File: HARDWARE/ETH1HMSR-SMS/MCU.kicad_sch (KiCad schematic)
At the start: 27 parts, among them J401 20021111-00010T4LF, U401 STM32H743VITx, U402 24LC08B-E/MS, Y401 NX5032GA-16

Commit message: SW and HW development
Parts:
- added C415, C418: 1u, Capacitor_SMD:C_0603_1608Metric_Pad1.08x0.95mm_HandSolder, symbol Device:C
- added C416, C417: 0.1u, Capacitor_SMD:C_0603_1608Metric_Pad1.08x0.95mm_HandSolder, symbol Device:C
- added R407: 0, Resistor_SMD:R_0603_1608Metric_Pad0.98x0.95mm_HandSolder, symbol Device:R
- added U403: ADR4533, Package_SO:SOIC-8_3.9x4.9mm_P1.27mm, symbol Reference_Voltage:ADR4533
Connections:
- net GND: now also C415.2, C416.2, C417.2, C418.2, U403.4 (GND)
- net MCU_DEFAULT: now also U401.77 (PA15); no longer U401.22 (PA0)
- net VDDA: now also R407.2; no longer U401.20 (VREF+)
- net HMSR_VOUT: now reaches U401.18 (PC3_C)
- new net +3.3VADC: C417.1, C418.1, R407.1, U401.20 (VREF+), U403.6 (OUT)
- new net +5V: C415.1, C416.1, U403.2 (IN)
- no-connect marks 32 -> 30
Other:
- moved on the sheet: C406, C409, C410, C412, FB401, JP401, R401, R403

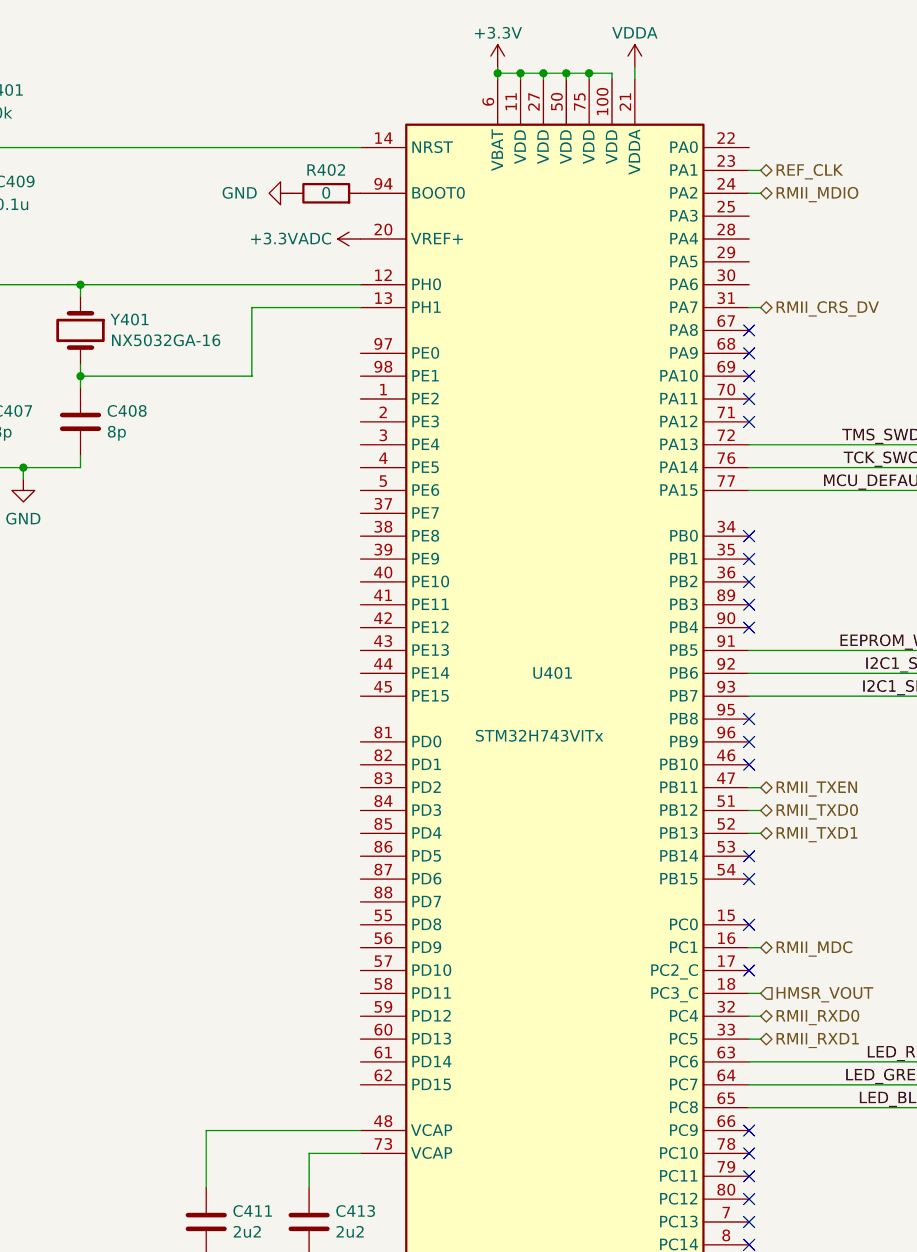
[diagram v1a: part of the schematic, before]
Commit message: Updated to Kicad 8
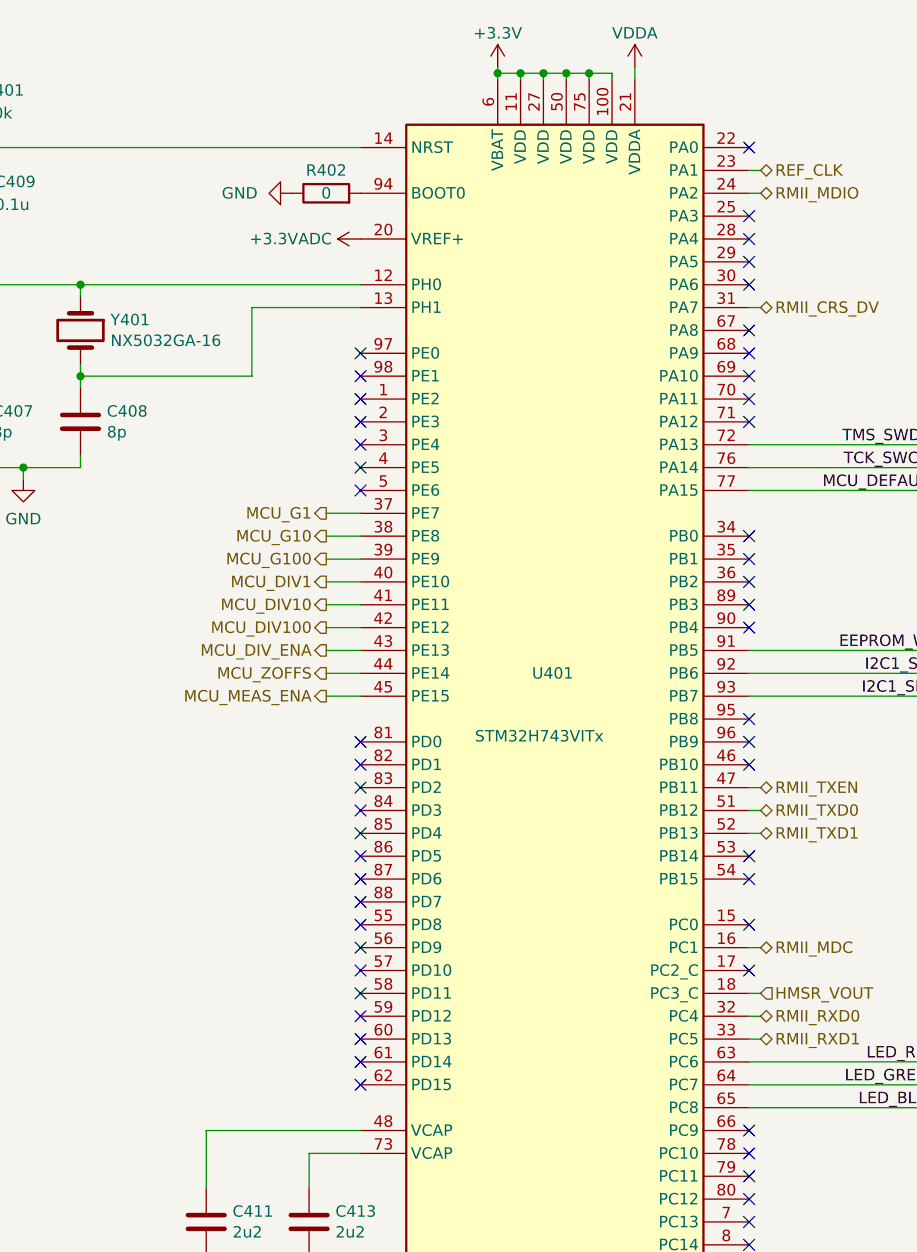
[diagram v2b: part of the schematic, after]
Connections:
- net MCU_G1: now reaches U401.37 (PE7)
- net MCU_G10: now reaches U401.38 (PE8)
- net MCU_G100: now reaches U401.39 (PE9)
- net MCU_DIV1: now reaches U401.40 (PE10)
- net MCU_DIV10: now reaches U401.41 (PE11)
- net MCU_DIV100: now reaches U401.42 (PE12)
- net MCU_DIV_ENA: now reaches U401.43 (PE13)
- net MCU_ZOFFS: now reaches U401.44 (PE14)
- net MCU_MEAS_ENA: now reaches U401.45 (PE15)
- no-connect marks 30 -> 58

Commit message: PCB design
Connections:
- net MCU_DEFAULT: no longer JP401.1 (A), R403.1, U401.77 (PA15)
- net MCU_DEF: now reaches U401.1 (PE2)
- net MCU_DEF: now also JP401.1 (A), R403.1
- no-connect marks 58 -> 57
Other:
- moved on the sheet: C401, C402, C403, C404, C405, C406, C407, C408, C409, C410, C411, C412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

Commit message: Development
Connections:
- net LED_BLUE: now also U401.63 (PC6); no longer U401.65 (PC8)
- net LED_GREEN: now also U401.65 (PC8); no longer U401.64 (PC7)
- net LED_RED: now also U401.64 (PC7); no longer U401.63 (PC6)
- net MCU_DIV1: now also U401.45 (PE15); no longer U401.40 (PE10)
- net MCU_DIV_ENA: now also U401.44 (PE14); no longer U401.43 (PE13)
- net MCU_G1: now also U401.40 (PE10); no longer U401.37 (PE7)
- net MCU_G100: now also U401.37 (PE7); no longer U401.39 (PE9)
- net MCU_MEAS_ENA: now also U401.39 (PE9); no longer U401.45 (PE15)
- net MCU_ZOFFS: now also U401.43 (PE13); no longer U401.44 (PE14)
- net OCD_EXT: now reaches U401.34 (PB0)
- net OCD_INT: now reaches U401.46 (PB10)
- no-connect marks 57 -> 56
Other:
- moved on the sheet: C406, C407, C408, C409, C410, C411, C412, C413, C414, C416, C417, C418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

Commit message: Development
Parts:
- removed R407: 0, Resistor_SMD:R_0603_1608Metric_Pad0.98x0.95mm_HandSolder, symbol Device:R
- removed U403: ADR4533, Package_SO:SOIC-8_3.9x4.9mm_P1.27mm, symbol Reference_Voltage:ADR4533
- added C409, C412: 0.1u, Capacitor_SMD:C_0603_1608Metric_Pad1.08x0.95mm_HandSolder, symbol Device:C
- added C411: 1u, Capacitor_SMD:C_0603_1608Metric_Pad1.08x0.95mm_HandSolder, symbol Device:C
- added R406: 0, Resistor_SMD:R_0603_1608Metric_Pad0.98x0.95mm_HandSolder, symbol Device:R
- added U401: LT6350xMS8, Package_SO:MSOP-8_3x3mm_P0.65mm, symbol ETH1HMSR-SMS:LT6350xMS8
- added U402: REF1933AIDDCT, Package_TO_SOT_SMD:TSOT-23-5_HandSoldering, symbol ETH1HMSR-SMS:REF1933AIDDCT
- renumbered C415 to C402, C402 to C403, C416 to C404, C417 to C405, C403 to C406, C418 to C407, C404 to C408, C405 to C410, C406 to C413, C409 to C414, C407 to C415, C408 to C416, C410 to C417, C411 to C418, C413 to C419, C412 to C420, C414 to C421, R403 to R401, R401 to R402, R402 to R403, U401 to U403, U402 to U404
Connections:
- net +3.3V: now also C412.1, U401.3 (V+), U401.7 (~{SHDN})
- net +3.3VADC: now also U402.5 (Vref)
- net +5V: now also U402.3 (EN), U402.4 (Vin)
- net GND: now also C409.2, C411.2, C412.2, U401.6 (V-), U402.2 (GND)
- net HMSR_VOUT: now also R406.1, U401.8 (+IN1); no longer U403.18 (PC3_C)
- net VOUTN: now reaches U403.17 (PC2_C)
- net VOUTN: now also U401.5 (OUT2)
- new net +1.65V: C409.1, C411.1, U401.2 (+IN2), U402.1 (Vbias)
- new net VOUTP: R406.2, U401.1 (-IN1), U401.4 (OUT1), U403.18 (PC3_C)
- no-connect marks 56 -> 55
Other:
- moved on the sheet: C402, C404, C405, C407, C413, C414, C415, C416, C417, C418, C419, C420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

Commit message: Development
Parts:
- added R407, R408: 0, Resistor_SMD:R_0603_1608Metric_Pad0.98x0.95mm_HandSolder, symbol Device:R
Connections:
- net MCU_G1: now also U403.36 (PB2); no longer U403.40 (PE10)
- net MCU_G10: now also U403.29 (PA5); no longer U403.38 (PE8)
- net MCU_G100: now also U403.28 (PA4); no longer U403.37 (PE7)
- net MCU_ZOFFS: now also U403.35 (PB1); no longer U403.43 (PE13)
- net VOUTN: now also R408.2; no longer U401.5 (OUT2)
- net VOUTP: now also R407.2; no longer R406.2, U401.1 (-IN1), U401.4 (OUT1)
- net +1.65V renamed VDD
- net VDD: no longer U402.1 (Vbias)
- net HMSR_VOUT renamed VOUT
- net MCU_DIV1: no longer names the net of U403.45 (PE15)
- net MCU_DIV10: no longer names the net of U403.41 (PE11)
- net MCU_DIV100: no longer names the net of U403.42 (PE12)
- net MCU_DIV_ENA: no longer names the net of U403.44 (PE14)
- net MCU_MEAS_ENA: no longer names the net of U403.39 (PE9)
- new net: R406.2, R407.1, U401.1 (-IN1), U401.4 (OUT1)
- new net: R408.1, U401.5 (OUT2)
- no-connect marks 55 -> 61

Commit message: development
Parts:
- R406: value 0 -> DNP; now not fitted
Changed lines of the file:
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@@
 	(wire
 		(pts
-			(xy 133.35 57.15) (xy 144.78 57.15)
+			(xy 134.62 57.15) (xy 144.78 57.15)
 		)
 		(stroke
@@
 	)
 	(label "MCU_DEF"
-		(at 133.35 57.15 0)
+		(at 134.62 57.15 0)
 		(fields_autoplaced yes)
 		(effects
@@
 		(in_bom yes)
 		(on_board yes)
-		(dnp no)
+		(dnp yes)
 		(property "Reference" "R406"
 			(at 48.26 54.864 90)
@@
 			)
 		)
-		(property "Value" "0"
+		(property "Value" "DNP"
 			(at 48.26 57.404 90)
 			(effects
